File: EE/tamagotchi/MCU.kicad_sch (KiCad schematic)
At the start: 5 parts, among them J7 TAG_CONNECT, U2 STM32G031G8Ux

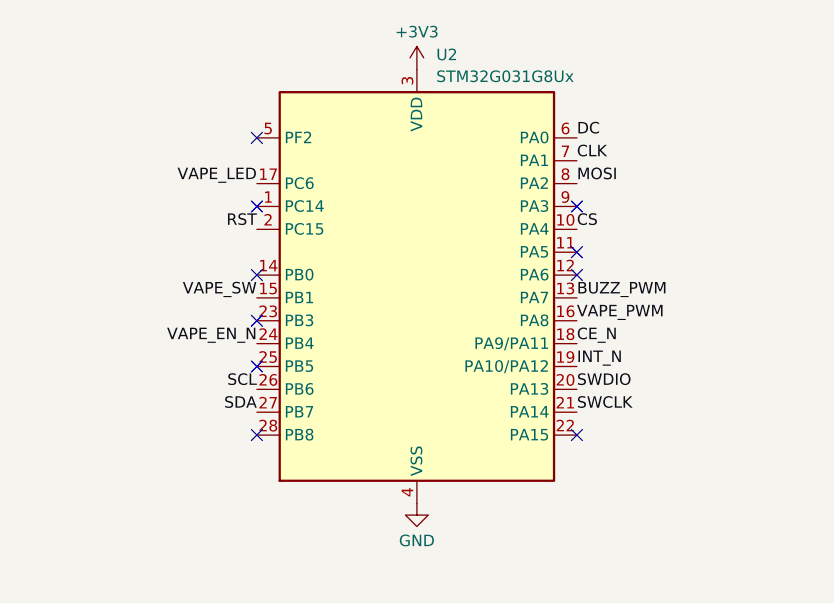
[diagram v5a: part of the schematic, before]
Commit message: Added pressure sensor. Re laid out board
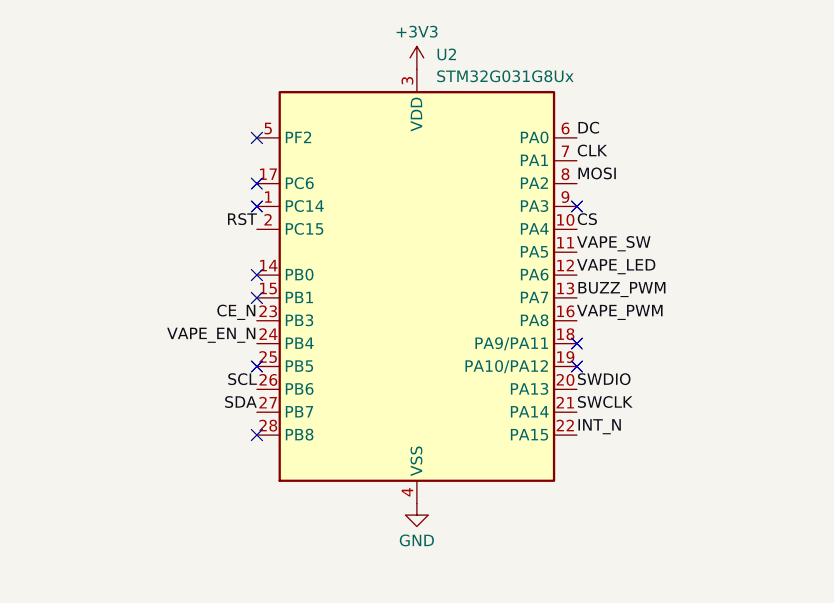
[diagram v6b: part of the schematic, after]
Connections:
- net CE_N: now also U2.23 (PB3); no longer U2.18 (PA9/PA11)
- net INT_N: now also U2.22 (PA15); no longer U2.19 (PA10/PA12)
- net VAPE_LED: now also U2.12 (PA6); no longer U2.17 (PC6)
- net VAPE_SW: now also U2.11 (PA5); no longer U2.15 (PB1)
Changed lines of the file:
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@@
 	(paper "A4")
 	(no_connect
+		(at 135.89 91.44)
+	)
+	(no_connect
+		(at 171.45 99.06)
+	)
+	(no_connect
 		(at 35.56 177.8)
 	)
 	(no_connect
+		(at 171.45 96.52)
+	)
+	(no_connect
 		(at 135.89 73.66)
 	)
 	(no_connect
-		(at 135.89 93.98)
-	)
-	(no_connect
-		(at 171.45 88.9)
-	)
-	(no_connect
 		(at 135.89 106.68)
 	)
@@
 	)
 	(no_connect
-		(at 171.45 86.36)
-	)
-	(no_connect
 		(at 35.56 182.88)
 	)
 	(no_connect
-		(at 171.45 106.68)
-	)
-	(no_connect
 		(at 135.89 81.28)
 	)
 	(no_connect
+		(at 135.89 78.74)
+	)
+	(no_connect
 		(at 171.45 81.28)
 	)
@@
 			(width 0)
 			(type default)
-		)
-	)
-	(label "CE_N"
-		(at 171.45 96.52 0)
-		(effects
-			(font
-				(size 1.27 1.27)
-			)
-			(justify left bottom)
 		)
 	)
@@
 		)
 	)
+	(label "INT_N"
+		(at 171.45 106.68 0)
+		(effects
+			(font
+				(size 1.27 1.27)
+			)
+			(justify left bottom)
+		)
+	)
+	(label "VAPE_LED"
+		(at 171.45 88.9 0)
+		(effects
+			(font
+				(size 1.27 1.27)
+			)
+			(justify left bottom)
+		)
+	)
 	(label "BUZZ_PWM"
 		(at 171.45 91.44 0)
@@
 		)
 	)
+	(label "VAPE_SW"
+		(at 171.45 86.36 0)
+		(effects
+			(font
+				(size 1.27 1.27)
+			)
+			(justify left bottom)
+		)
+	)
 	(label "CLK"
 		(at 171.45 76.2 0)
@@
 		)
 	)
-	(label "INT_N"
-		(at 171.45 99.06 0)
-		(effects
-			(font
-				(size 1.27 1.27)
-			)
-			(justify left bottom)
-		)
-	)
 	(label "MOSI"
 		(at 171.45 78.74 0)
@@
 		)
 	)
-	(label "VAPE_LED"
-		(at 135.89 78.74 180)
-		(effects
-			(font
-				(size 1.27 1.27)
-			)
-			(justify right bottom)
-		)
-	)
-	(label "VAPE_SW"
-		(at 135.89 91.44 180)
-		(effects
-			(font
+	(label "CE_N"
+		(at 135.89 93.98 180)
+		(effects
+			(font
